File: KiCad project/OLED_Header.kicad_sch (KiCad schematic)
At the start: 1 part, among them J9 Conn_01x04_Socket

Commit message: Unify 3.3V power nets; update PCB netlist
The HX711 sheet used power:+3.3V (4 symbols) and the OLED header sheet
used power:+3V3, which are separate nets from the SparkFun 3.3V symbol
used on the root, ESP32-C3 and UI sheets. The HX711 (VSUP/AVDD/DVDD,
decoupling, E+ net tie) and the OLED VCC pin were therefore unpowered.
Changed the five symbols' Value to 3.3V so they join the LDO rail:
one 3.3V net with 25 pins. ERC: 0 errors (87 library warnings, as before).

Updated PCB from schematic: +3.3V/+3V3 nets gone, 66 nets, 138 unrouted
connections (was 136). KiCad also normalized symbol-instance project
names in all sheets from the old KLP-5e parent names.

Co-Authored-By: Claude Fable 5.1 <noreply@anthropic.com>
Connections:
- net +3V3 renamed 3.3V
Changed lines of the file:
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@@
 		)
 		(instances
-			(project ""
+			(project "ScaleController_RevA"
 				(path "/16c571a0-8550-4f05-972c-22b0701cbf02/215dc542-b8c7-4909-b854-34402cacdf29"
 					(reference "#FLG09")
@@
 		)
 		(instances
-			(project ""
+			(project "ScaleController_RevA"
 				(path "/16c571a0-8550-4f05-972c-22b0701cbf02/215dc542-b8c7-4909-b854-34402cacdf29"
 					(reference "J9")
@@
 		)
 		(instances
-			(project ""
+			(project "ScaleController_RevA"
 				(path "/16c571a0-8550-4f05-972c-22b0701cbf02/215dc542-b8c7-4909-b854-34402cacdf29"
 					(reference "#PWR034")
@@
 			)
 		)
-		(property "Value" "+3V3"
+		(property "Value" "3.3V"
 			(at 86.36 64.7699 90)
 			(effects
@@
 		)
 		(instances
-			(project ""
+			(project "ScaleController_RevA"
 				(path "/16c571a0-8550-4f05-972c-22b0701cbf02/215dc542-b8c7-4909-b854-34402cacdf29"
 					(reference "#PWR033")

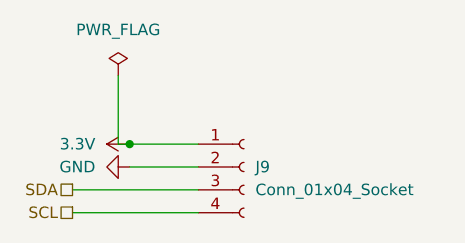
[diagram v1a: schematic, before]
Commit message: OLED header J9 on the back side with the module's pin order
J9 rewired to 1=GND 2=3V3 3=SCL 4=SDA (the order on the 0.96in Hosyond
I2C module) and flipped to the bottom side, so the module plugs in from
below and lies flat under the board, clear of the load-cell sockets.
SCL/SDA tails re-routed to the swapped pads; 3V3/GND land on the planes.
J9 labels reordered on top and duplicated mirrored on the back. The
DISP1 placeholder now models the 0.96in module (27 x 27.5 mm) under the
board, replacing the 1.3in upright placeholder.

Fills stale in this commit (refill in GUI). Enclosure note: standoffs
under the board need >= 14 mm for the module.

Co-Authored-By: Claude Fable 5.1 <noreply@anthropic.com>
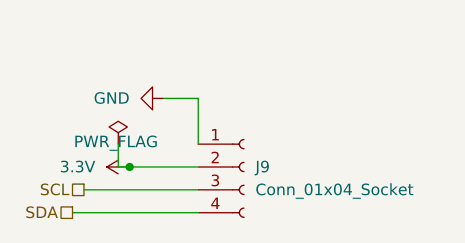
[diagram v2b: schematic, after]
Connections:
- net 3.3V: now also J9.2 (Pin_2); no longer J9.1 (Pin_1)
- net GND: now also J9.1 (Pin_1); no longer J9.2 (Pin_2)
- net SCL: now also J9.3 (Pin_3); no longer J9.4 (Pin_4)
- net SDA: now also J9.4 (Pin_4); no longer J9.3 (Pin_3)
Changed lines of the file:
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@@
 	)
 	(junction
-		(at 90.17 64.77)
+		(at 90.17 67.31)
 		(diameter 0)
 		(color 0 0 0 0)
@@
 	(wire
 		(pts
-			(xy 83.82 69.85) (xy 97.79 69.85)
-		)
-		(stroke
-			(width 0)
-			(type default)
-		)
-	)
-	(wire
-		(pts
-			(xy 90.17 64.77) (xy 97.79 64.77)
-		)
-		(stroke
-			(width 0)
-			(type default)
-		)
-	)
-	(wire
-		(pts
-			(xy 88.9 64.77) (xy 90.17 64.77)
-		)
-		(stroke
-			(width 0)
-			(type default)
-		)
-	)
-	(wire
-		(pts
-			(xy 88.9 57.15) (xy 88.9 64.77)
+			(xy 85.09 69.85) (xy 97.79 69.85)
+		)
+		(stroke
+			(width 0)
+			(type default)
+		)
+	)
+	(wire
+		(pts
+			(xy 90.17 67.31) (xy 97.79 67.31)
+		)
+		(stroke
+			(width 0)
+			(type default)
+		)
+	)
+	(wire
+		(pts
+			(xy 97.79 59.69) (xy 97.79 64.77)
+		)
+		(stroke
+			(width 0)
+			(type default)
+		)
+	)
+	(wire
+		(pts
+			(xy 88.9 67.31) (xy 90.17 67.31)
+		)
+		(stroke
+			(width 0)
+			(type default)
+		)
+	)
+	(wire
+		(pts
+			(xy 88.9 64.77) (xy 88.9 67.31)
 		)
 		(stroke
@@
 	(wire
 		(pts
-			(xy 90.17 67.31) (xy 97.79 67.31)
+			(xy 97.79 59.69) (xy 93.98 59.69)
 		)
 		(stroke
@@
 	)
 	(hierarchical_label "SDA"
-		(shape passive)
-		(at 83.82 69.85 180)
-		(effects
-			(font
-				(size 1.27 1.27)
-			)
-			(justify right)
-		)
-	)
-	(hierarchical_label "SCL"
 		(shape passive)
 		(at 83.82 72.39 180)
@@
 		)
 	)
+	(hierarchical_label "SCL"
+		(shape passive)
+		(at 85.09 69.85 180)
+		(effects
+			(font
+				(size 1.27 1.27)
+			)
+			(justify right)
+		)
+	)
 	(symbol
 		(lib_id "power:PWR_FLAG")
-		(at 88.9 57.15 0)
+		(at 88.9 64.77 0)
 		(unit 1)
 		(exclude_from_sim no)
@@
 		(on_board yes)
 		(dnp no)
-		(fields_autoplaced yes)
 		(property "Reference" "#FLG09"
-			(at 88.9 55.245 0)
+			(at 88.9 62.865 0)
 			(effects
 				(font
@@
 		)
 		(property "Value" "PWR_FLAG"
-			(at 88.9 52.07 0)
+			(at 88.646 64.516 0)
 			(effects
 				(font
@@
 		)
 		(property "Footprint" ""
-			(at 88.9 57.15 0)
+			(at 88.9 64.77 0)
 			(effects
 				(font
@@
 		)
 		(property "Datasheet" "~"
-			(at 88.9 57.15 0)
+			(at 88.9 64.77 0)
 			(effects
 				(font
@@
 		)
 		(property "Description" "Special symbol for telling ERC where power comes from"
-			(at 88.9 57.15 0)
+			(at 88.9 64.77 0)
 			(effects
 				(font
@@
 	(symbol
 		(lib_id "power:GND")
-		(at 90.17 67.31 270)
+		(at 93.98 59.69 270)
 		(unit 1)
 		(exclude_from_sim no)
@@
 		(on_board yes)
 		(dnp no)
-		(fields_autoplaced yes)
 		(property "Reference" "#PWR034"
-			(at 83.82 67.31 0)
+			(at 87.63 59.69 0)
 			(effects
 				(font
@@
 		)
 		(property "Value" "GND"
-			(at 86.36 67.3099 90)
+			(at 90.17 59.6899 90)
 			(effects
 				(font
@@
 		)
 		(property "Footprint" ""
-			(at 90.17 67.31 0)
+			(at 93.98 59.69 0)
 			(effects
 				(font
@@
 		)
 		(property "Datasheet" ""
-			(at 90.17 67.31 0)
+			(at 93.98 59.69 0)
 			(effects
 				(font
@@
 		)
 		(property "Description" "Power symbol creates a global label with name \"GND\" , ground"
-			(at 90.17 67.31 0)
+			(at 93.98 59.69 0)
 			(effects
 				(font
@@
 	(symbol
 		(lib_id "power:+3V3")
-		(at 90.17 64.77 90)
+		(at 90.17 67.31 90)
 		(unit 1)
 		(exclude_from_sim no)
@@
 		(fields_autoplaced yes)
 		(property "Reference" "#PWR033"
-			(at 93.98 64.77 0)
+			(at 93.98 67.31 0)
 			(effects
 				(font
@@
 		)
 		(property "Value" "3.3V"
-			(at 86.36 64.7699 90)
+			(at 86.36 67.3099 90)
 			(effects
 				(font
@@
 		)
 		(property "Footprint" ""
-			(at 90.17 64.77 0)
+			(at 90.17 67.31 0)
 			(effects
 				(font
@@
 		)
 		(property "Datasheet" ""
-			(at 90.17 64.77 0)
+			(at 90.17 67.31 0)
 			(effects
 				(font
@@
 		)
 		(property "Description" "Power symbol creates a global label with name \"+3V3\""
-			(at 90.17 64.77 0)
-			(effects
-				(font
+			(at 90.17 67.31 0)
+			(effects
+				(font

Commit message: Schematic: title blocks (Scale Controller, rev A, 2026-09-18, per-sheet comments); replace stale CP2102 and ESP32-S3 notes
Co-Authored-By: Claude Fable 5.1 <noreply@anthropic.com>
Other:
- company: (none) -> Steve Maegley
- title: ESP32 sensor board -> Scale Controller
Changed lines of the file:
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@@
 	(paper "A4")
 	(title_block
-		(title "ESP32 sensor board")
-		(rev "1")
-		(comment 1 "OLED Header")
+		(title "Scale Controller")
+		(date "2026-09-18")
+		(rev "A")
+		(company "Steve Maegley")
+		(comment 1 "OLED header J9")
 	)
 	(junction
